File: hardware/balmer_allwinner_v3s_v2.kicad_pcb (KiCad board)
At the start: 4 copper layers, 60 x 60 mm, 120 parts, among them J1 JAE_SIM_Card_SF72S006, J11 Micro_SD_Card, J2 UART, J3 Bus_PCI_Express_Mini, J4 USB_C_Receptacle, J8 HR911105_RJ45, SW2 SW_MEC_5G, U1 AllwinnerV3S, U10 TLV62568DBV, U2 CH340C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

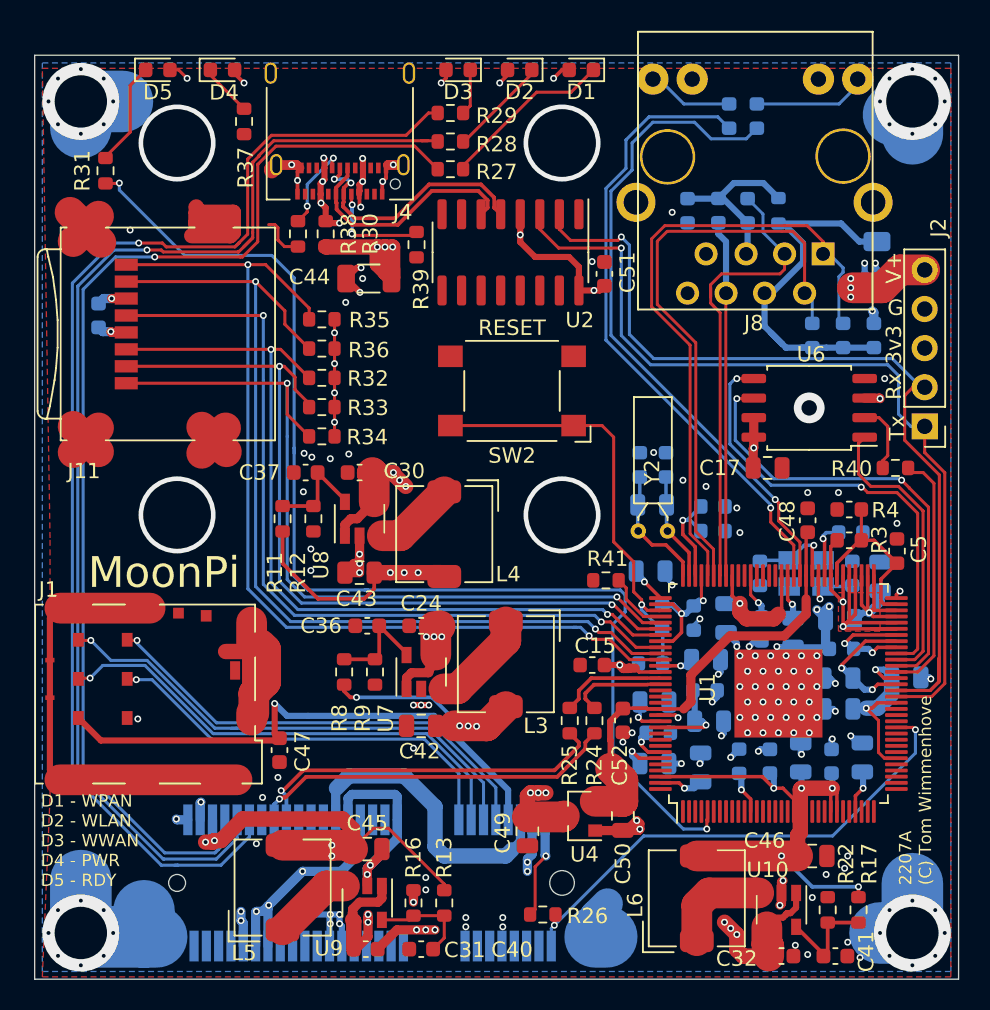
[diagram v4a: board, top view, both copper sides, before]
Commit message: Move Y1 to top-layer
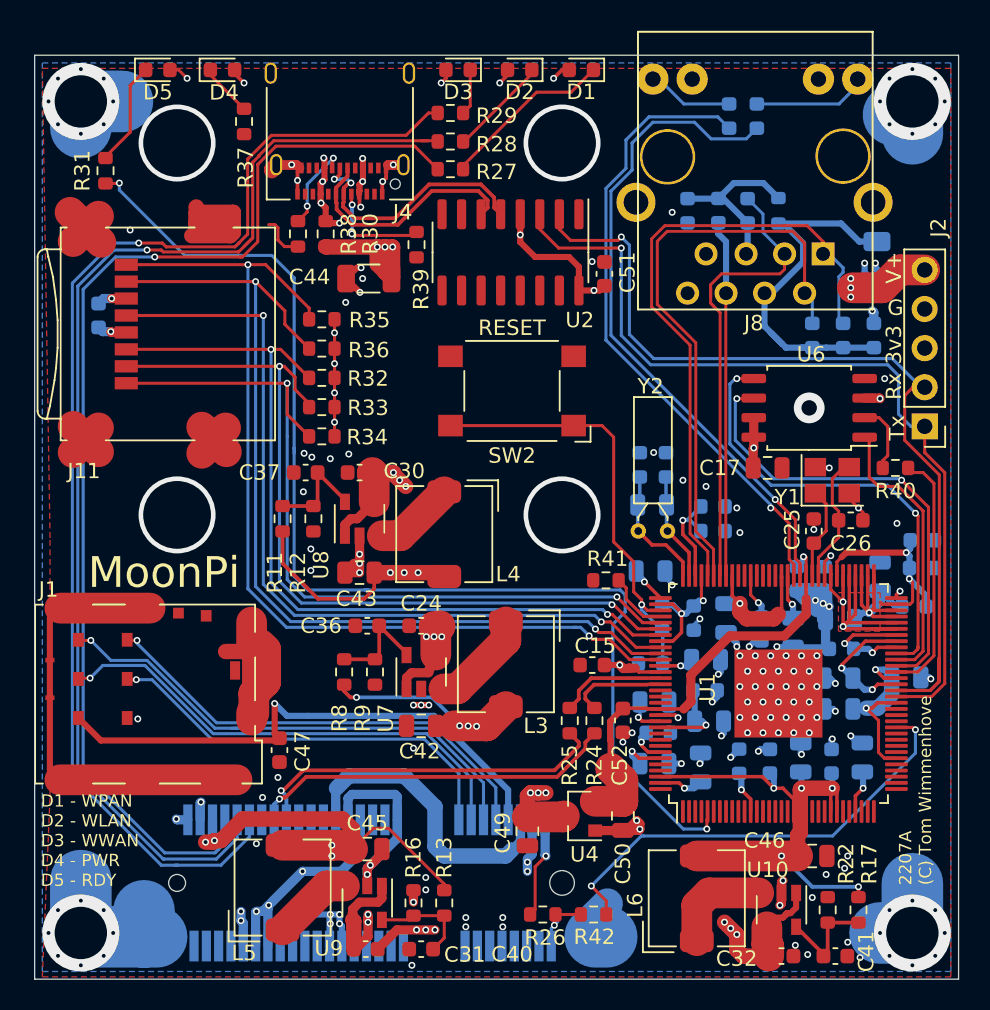
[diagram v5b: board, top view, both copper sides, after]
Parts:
- added R42: 0R, Resistor_SMD:R_0603_1608Metric, F.Cu at (98.3, 130.8)
- C25, C26: value 18 -> 18p; moved to F.Cu
- C28, C29: value 18 -> 18p
- C48, C5, R3, R4: moved to B.Cu
- L1: value 600Z -> 10uH
- R14, R15: value 1K -> 200R
- R30: value 0 -> 0R
- Y1: moved to F.Cu
- moved Y1 6.28 mm to (113.8, 102.6)
- moved R3 6.01 mm to (119.1, 110.8)
- moved R4 5.15 mm to (119.7, 106.5), turned to 0 degrees
- moved C25 4.45 mm to (112.6, 105.9), turned to 90 degrees
- moved C48 3.86 mm to (111.5, 109.0), turned to 270 degrees
- moved C26 3.45 mm to (115.0, 105.2), turned to 0 degrees
- moved R1 3.45 mm to (113.3, 109.0), turned to 90 degrees
- moved C5 1.94 mm to (119.6, 108.3), turned to 0 degrees
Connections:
- J3 pad 1: WAKE -> Net-(J3-Pad1)
- R26 pad 2: WAKE -> Net-(J3-Pad1)
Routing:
- net GND: track 188.2 -> 197.4 mm, vias 168 -> 171
- net Net-(J3-Pad1): track 0.00 -> 4.13 mm, vias 0 -> 1
- net X24MOUT: track 4.38 -> 8.41 mm, vias 1 -> 0
- net WAKE: track 33.1 -> 29.7 mm
- net /SVREF: track 12.1 -> 14.4 mm, vias 0 -> 2
- net Net-(R1-Pad2): track 3.72 -> 2.33 mm
- net +3V0: track 30.0 -> 29.3 mm, vias 0 -> 1
- net +1V8: track 84.9 -> 85.6 mm
- net SPI_CS: track 18.8 -> 18.2 mm
- net X24MIN: track 5.94 -> 6.00 mm, vias 1 -> 0

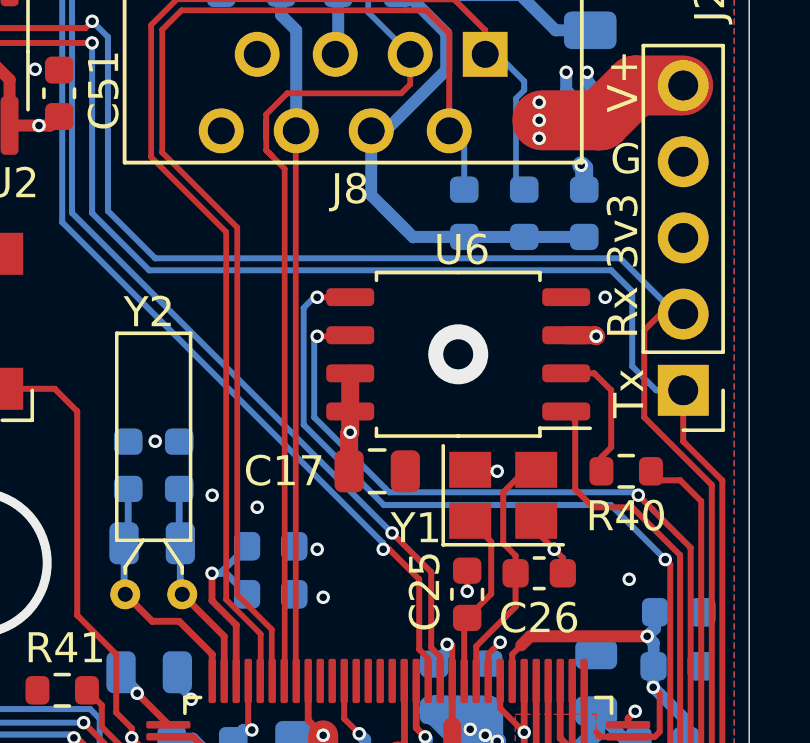
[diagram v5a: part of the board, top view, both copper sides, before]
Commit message: Improved spacing
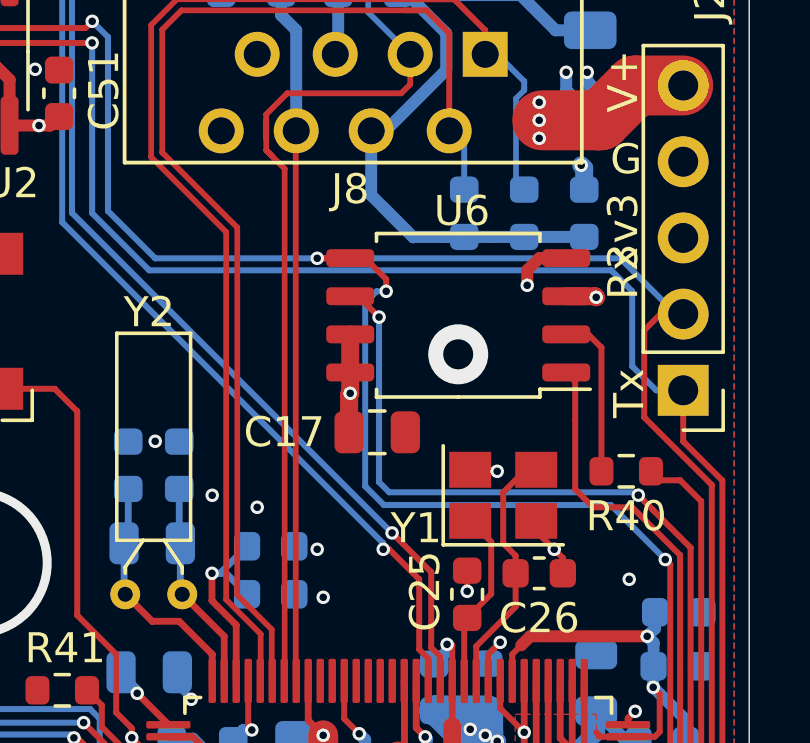
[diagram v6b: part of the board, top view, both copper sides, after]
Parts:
- moved U6 1.30 mm to (112.3, 96.6)
- moved C17 1.30 mm to (109.6, 100.5)
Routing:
- net GND: track 197.4 -> 199.4 mm
- net SPI_CS: track 18.2 -> 20.1 mm
- net SPI_MOSI: track 29.9 -> 31.5 mm, vias 2 -> 3

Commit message: Minor layout changes
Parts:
- moved R3 0.40 mm to (119.5, 110.8)
- moved C33 0.36 mm to (116.3, 92.9)
- moved R18 0.36 mm to (114.3, 92.9)
- moved R19 0.36 mm to (112.3, 92.9)
- moved C17 0.30 mm to (109.6, 100.8)
- moved C26 0.30 mm to (115.3, 105.2)
- moved Y1 0.30 mm to (113.8, 102.3)
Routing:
- net UART0_TX: track 56.8 -> 78.1 mm, vias 1 -> 2
- net EPHY-LINK-LED: track 43.1 -> 36.6 mm, vias 1 -> 3
- net EPHY-SPD-LED: track 41.6 -> 36.2 mm, vias 1 -> 3
- net GND: track 199.4 -> 204.0 mm, vias 171 -> 173
- net UART0_RX: track 58.9 -> 61.8 mm, vias 1 -> 2
- net VCC: track 191.2 -> 193.7 mm
- net EPHY-TXP: track 41.5 -> 39.1 mm
- net EPHY-TXN: track 38.8 -> 36.8 mm
- net Net-(C33-Pad1): track 25.2 -> 23.3 mm
- net X24MOUT: track 8.41 -> 9.40 mm
- net SPI_CS: track 20.1 -> 21.0 mm
- net +1V8: track 85.6 -> 86.4 mm
- net +3V3: track 174.0 -> 174.7 mm
- net SPI_SCK: track 30.0 -> 29.4 mm
- net SPI_MOSI: track 31.5 -> 31.4 mm, vias 3 -> 2

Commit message: Ready for JLCPCB
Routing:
- net UART0_TX: track 78.1 -> 60.1 mm
- net GND: track 204.0 -> 214.5 mm, vias 173 -> 172
- net Net-(J3-Pad44): track 77.6 -> 74.0 mm
- net Net-(J3-Pad42): track 79.4 -> 76.7 mm
- net Net-(J3-Pad46): track 75.2 -> 72.5 mm
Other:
- board text added: "2212A (C) Tom Wimmenhove"
- board text removed: "2207A (C) Tom Wimmenhove"
